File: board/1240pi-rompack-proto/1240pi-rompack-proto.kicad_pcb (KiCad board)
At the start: 2 copper layers, 76.2 x 97.8 mm, 39 parts, among them J20 CardEdge_ROMPACK, J21 Conn_02x09, J22 Conn_01x09, J23 Conn_01x09, J30 62684-50210, J31 Conn_02x09, J32 Conn_01x09, J33 Conn_02x09, J34 Conn_01x09, U10 AMS1117-3.3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

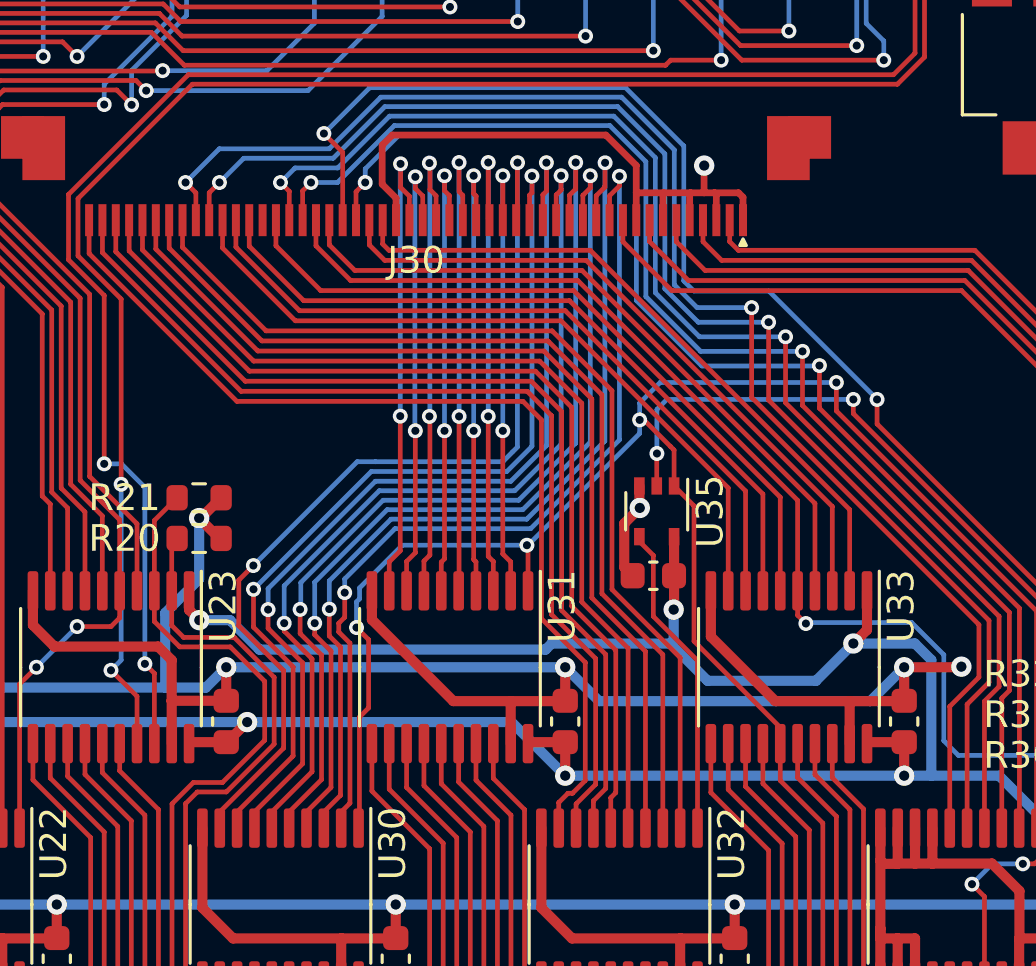
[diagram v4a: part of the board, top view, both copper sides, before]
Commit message: Move around A8..15 vias.
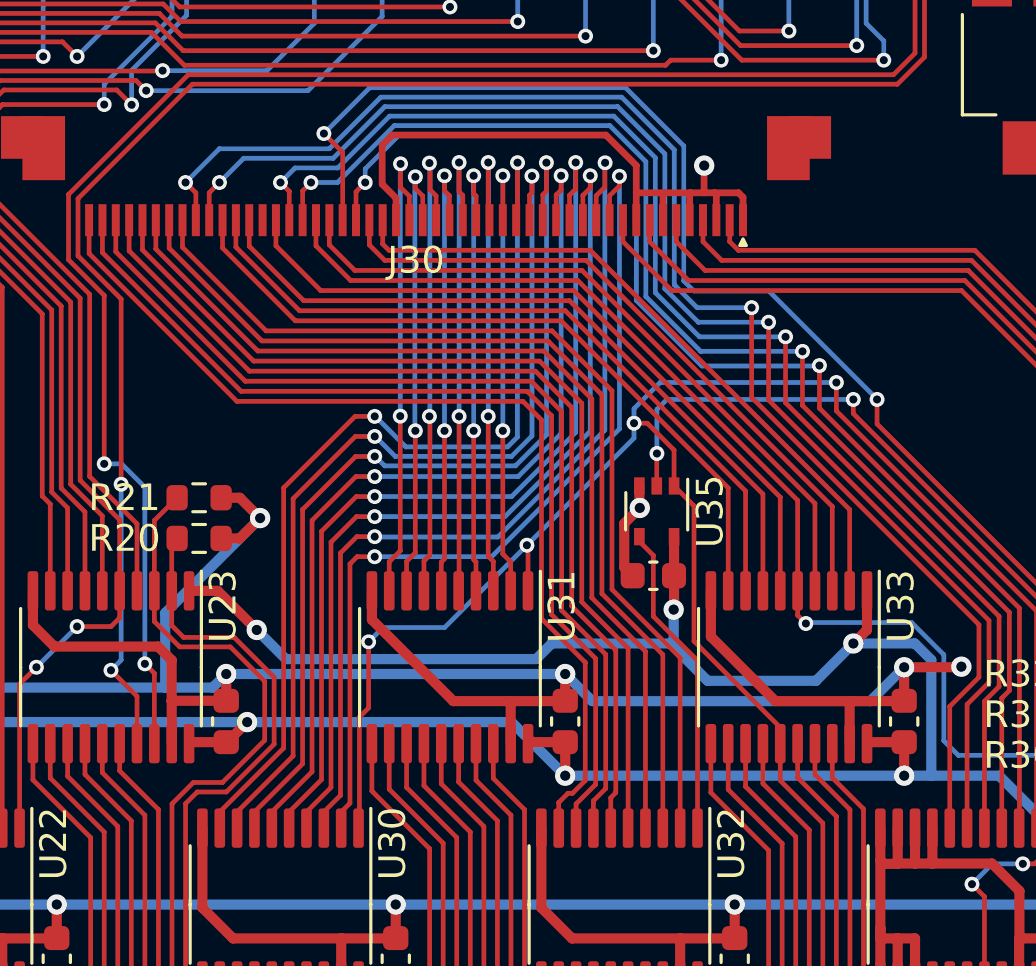
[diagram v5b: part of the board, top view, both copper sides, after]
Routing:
- net /IO Proc Bus/IOB_~{BUSACK}: track 122.3 -> 120.7 mm
- net GND: track 589.6 -> 591.1 mm

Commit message: Add voltage labels.
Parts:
- added REF**: Symbol_Warning_50mil, 0Local:Symbol_Warning_50mil, F.Cu at (177.8, 157.5)
- moved REF** 2.09 mm to (137.3, 119.9)
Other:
- board text added: "5V"
- board text added: "All signals 3.3V LVCMOS except Display"

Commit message: Fix names of BUSRQ and IORQ nets.
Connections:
- net /IO Proc Bus/IOB_~{IOREQ} renamed /IO Proc Bus/IOB_~{IORQ}
- net /IO Proc Bus/IO_~{BUSREQ} renamed /IO Proc Bus/IO_~{BUSRQ}
- net /IO Proc Bus/IO_~{IOREQ} renamed /IO Proc Bus/IO_~{IORQ}
- J33 pad 11: /IO Proc Bus/IOB_~{BUSACK} -> /IO Proc Bus/IOB_~{CLK}
- J33 pad 14: GND -> /IO Proc Bus/IOB_~{BUSRQ}
- J33 pad 16: /IO Proc Bus/IOB_~{CLK} -> GND
- J33 pad 9: /IO Proc Bus/IOB_~{BUSREQ} -> /IO Proc Bus/IOB_~{BUSACK}
- R32 pad 2: /IO Proc Bus/IOB_~{BUSREQ} -> /IO Proc Bus/IOB_~{BUSRQ}
- U36 pad 2: /IO Proc Bus/IOB_~{BUSREQ} -> /IO Proc Bus/IOB_~{BUSRQ}
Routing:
- net /IO Proc Bus/IOB_~{BUSREQ}: track 71.8 -> 0.00 mm
- net /IO Proc Bus/IOB_~{BUSRQ}: track 0.00 -> 67.3 mm
- net /IO Proc Bus/IOB_~{CLK}: track 62.4 -> 55.5 mm
- net /IO Proc Bus/IOB_~{BUSACK}: track 120.7 -> 118.1 mm
- net GND: track 591.1 -> 588.8 mm
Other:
- board text added: "~{BUSRQ}"
- board text added: "~{IORQ}"
- board text removed: "~{BUSREQ}"
- board text removed: "~{IOREQ}"

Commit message: Add bonsai logo to boards.
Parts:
- added G***: LOGO, 0Local:Symbol_Bonsai_6.7mm, F.Cu at (130.6, 119.9)
